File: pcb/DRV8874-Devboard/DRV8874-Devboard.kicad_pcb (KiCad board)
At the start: 4 copper layers, 65 x 67 mm, 53 parts, among them J1 Conn_01x04_Pin, J10 Conn_01x06_Pin, J12 Conn_01x03_Pin, J2 Screw_Terminal_01x02, J3 Conn_01x03_Pin, J4 Conn_01x03_Pin, J5 Conn_01x04_Pin, J6 Conn_01x03_Pin, J7 Conn_01x03_Pin, J9 Conn_01x03_Pin, U1 DRV8874, U2 BL9342, U3 DRV8874, U4 SN65HVD230, U5 TPS16630PWPR, U6 M95320-WMN6TP, U7 TinyThinker_J1

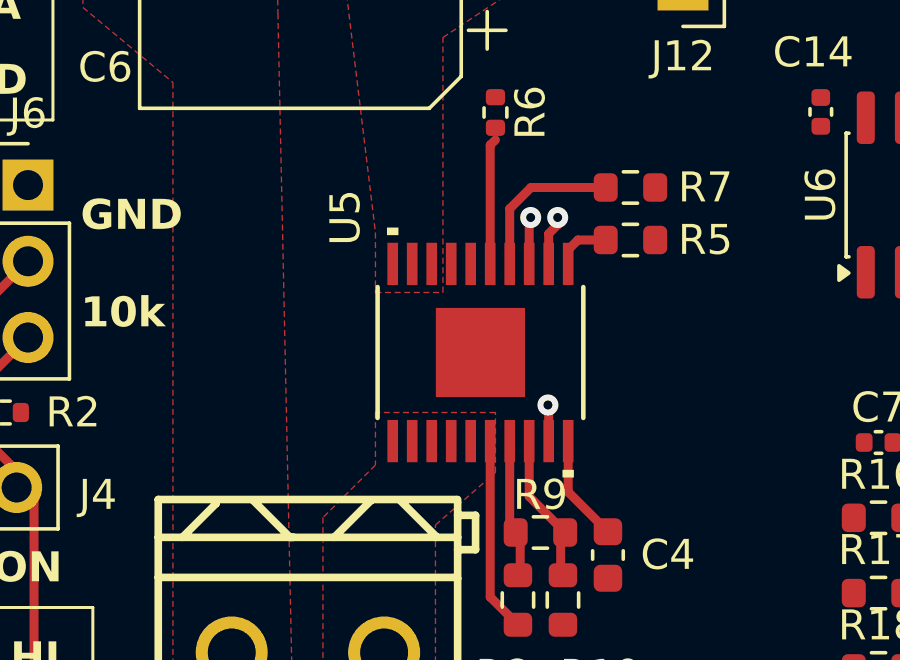
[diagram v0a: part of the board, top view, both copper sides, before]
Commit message: updated rotation offsets
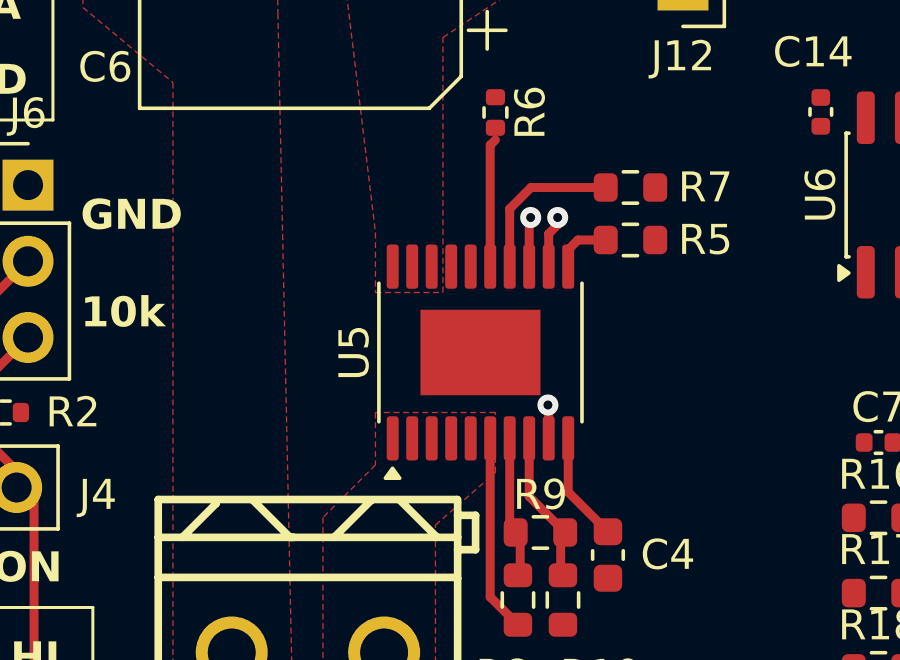
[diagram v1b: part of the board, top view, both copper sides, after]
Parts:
- U5: footprint Custom_Library:HTSSOP20_PWP_TEX -> Package_SO:HTSSOP-20-1EP_4.4x6.5mm_P0.65mm_EP2.85x4mm

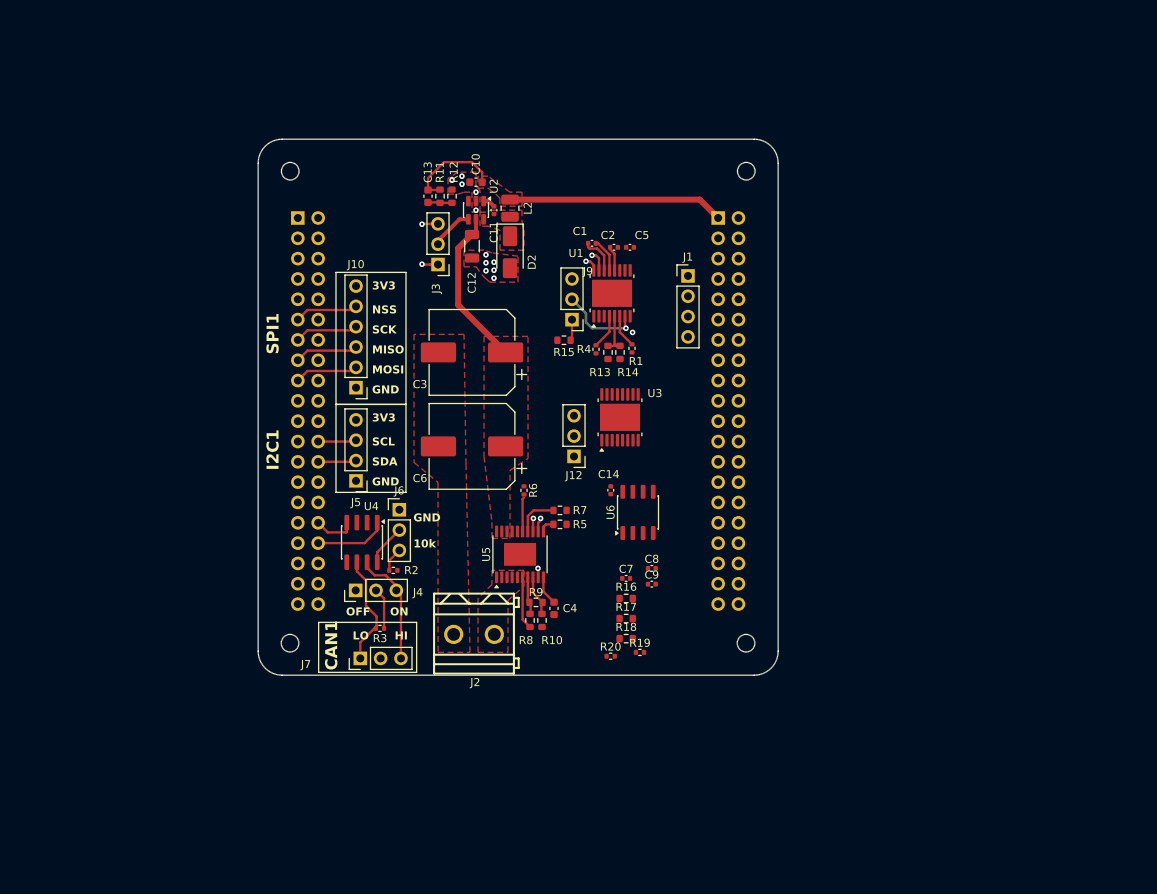
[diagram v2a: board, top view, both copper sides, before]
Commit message: routed major chunk of DRV8874 pair
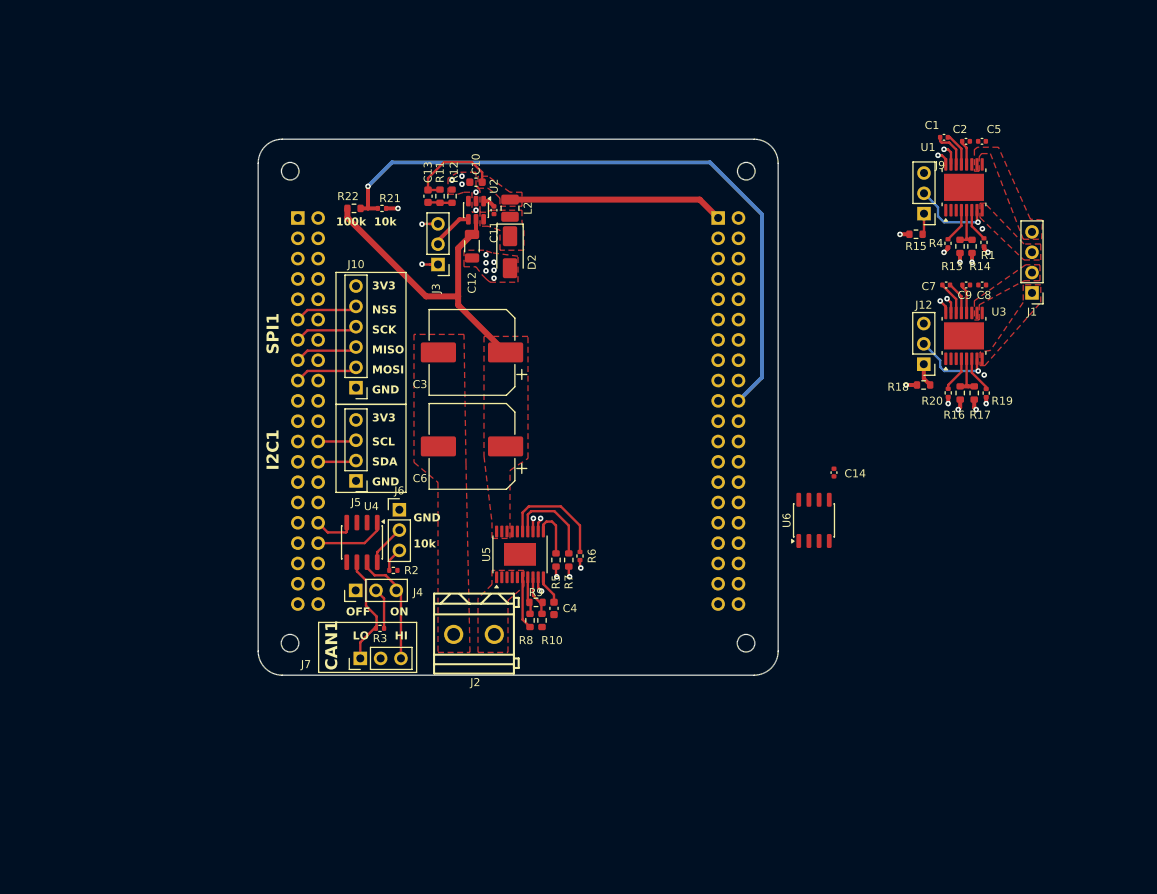
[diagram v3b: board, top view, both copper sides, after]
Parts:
- added R21: 10k, Resistor_SMD:R_0402_1005Metric, F.Cu at (112.2, 48.2)
- added R22: 100k, Resistor_SMD:R_0603_1608Metric, F.Cu at (108.8, 48.2)
- moved C8 54.4 mm to (187.3, 57.8)
- moved C7 54.3 mm to (182.8, 57.8), turned to 180 degrees
- moved C9 54.2 mm to (185.3, 57.8), turned to 180 degrees
- moved R19 54.1 mm to (187.8, 71.3), turned to -90 degrees
- moved R20 53.5 mm to (183.0, 71.3), turned to 90 degrees
- moved R17 51.8 mm to (186.3, 71.3), turned to -90 degrees
- moved R16 49.0 mm to (184.5, 71.3), turned to 90 degrees
- moved R18 48.9 mm to (179.9, 70.3), turned to 180 degrees
- moved C1 46.0 mm to (182.5, 39.4)
- moved C2 46.0 mm to (185.2, 39.9)
- moved C5 46.0 mm to (187.2, 39.9)
- moved J9 46.0 mm to (180.0, 48.9)
- moved R1 46.0 mm to (187.5, 52.5)
- moved R13 46.0 mm to (184.5, 53.0)
- moved R14 46.0 mm to (186.0, 53.0)
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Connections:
- J1 pad 1: /B_OUT- -> /B_OUT+
- J1 pad 2: /A_OUT- -> /B_OUT-
- J1 pad 3: /B_OUT+ -> /A_OUT+
- J1 pad 4: /A_OUT+ -> /A_OUT-
- U7 pad 20: unconnected-(U7A-ADC1_IN8-Pad20) -> /ADC_VSENSE
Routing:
- net /ADC_VSENSE: track 0.00 -> 82.3 mm, vias 0 -> 1
- net +BATT_PROT: track 19.8 -> 38.9 mm
- net GND: track 7.44 -> 21.1 mm, vias 16 -> 27
- net /B_IMODE: track 0.00 -> 10.3 mm, vias 0 -> 1
- net /TPS_FLT: track 4.21 -> 14.1 mm
- net +3.3V: track 5.42 -> 12.4 mm, vias 3 -> 9
- net /TPS_MON: track 5.33 -> 11.6 mm
- net /B_VREF: track 0.00 -> 5.28 mm
- net /TPS_ILIM: track 1.86 -> 6.75 mm
- net /B_IRPOPI: track 0.00 -> 4.52 mm
- net /B_nFault: track 0.00 -> 4.44 mm
- net /B_CPL: track 0.00 -> 4.23 mm
- net /B_CPH: track 0.00 -> 4.10 mm
- net /B_VCP: track 0.00 -> 3.72 mm
- net /B_IMODE_R: track 0.00 -> 2.93 mm
- added copper zone on F.Cu, net /A_OUT+
- added copper zone on F.Cu, net /A_OUT-
- added copper zone on F.Cu, net /B_OUT+
- added copper zone on F.Cu, net /B_OUT-
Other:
- board text added: "100k"

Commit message: moved DRV8874 pair onto the board
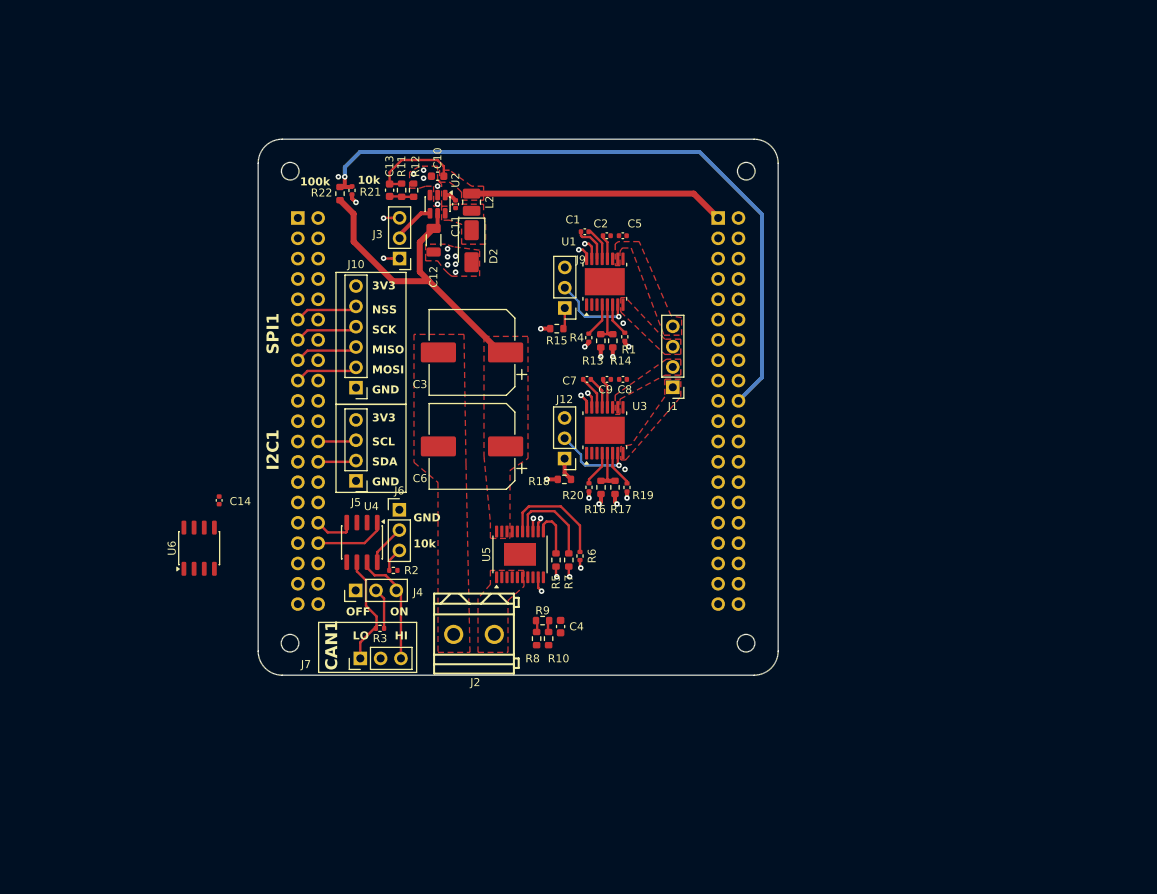
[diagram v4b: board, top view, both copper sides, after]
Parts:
- moved C14 76.9 mm to (91.9, 84.7)
- moved U6 76.9 mm to (89.4, 90.7)
- moved J12 46.4 mm to (135.1, 79.5)
- moved C1 46.4 mm to (137.6, 51.2)
- moved C2 46.4 mm to (140.3, 51.7)
- moved C5 46.4 mm to (142.3, 51.7)
- moved C7 46.4 mm to (137.9, 69.6)
- moved C8 46.4 mm to (142.4, 69.6)
- moved C9 46.4 mm to (140.4, 69.6)
- moved J1 46.4 mm to (148.6, 70.6)
- moved J9 46.4 mm to (135.1, 60.7)
- moved R1 46.4 mm to (142.6, 64.3)
- moved R13 46.4 mm to (139.6, 64.8)
- moved R14 46.4 mm to (141.1, 64.8)
- moved R15 46.4 mm to (134.1, 63.3)
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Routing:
- net +BATT_RAW: track 6.51 -> 0.00 mm
- net +5V: track 39.3 -> 44.0 mm
- net /TPS_OVP: track 5.30 -> 1.56 mm
- net /TPS_DVDT: track 3.57 -> 0.00 mm
- net /TPS_UVLO: track 4.69 -> 1.85 mm
- net /ADC_VSENSE: track 82.3 -> 84.7 mm
- net +BATT_PROT: track 38.9 -> 40.3 mm
- net GND: track 21.1 -> 20.8 mm, vias 27 -> 28

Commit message: checkpoint
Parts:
- moved U6 54.1 mm to (143.2, 96.7)
- moved C14 53.7 mm to (145.3, 90.6)
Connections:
- U7 pad 29: unconnected-(U7A-TIM2_CH4-Pad29) -> /A_IN1
- U7 pad 32: unconnected-(U7A-TIM2_CH1-Pad32) -> /A_IN2
- U7 pad 33: unconnected-(U7A-TIM2_CH2-Pad33) -> /B_IN1
- U7 pad 36: unconnected-(U7A-TIM2_CH3-Pad36) -> /B_IN2

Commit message: changed color of phase B net
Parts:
- moved C14 7.53 mm to (145.5, 98.1)
- moved U6 1.84 mm to (142.0, 98.1)
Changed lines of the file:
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@@
 	(footprint "Package_SO:SO-8_3.9x4.9mm_P1.27mm"
 		(layer "F.Cu")
-		(at 143.2 96.7 90)
+		(at 142 98.1 90)
 		(descr "SO, 8 Pin (https://www.nxp.com/docs/en/data-sheet/PCF8523.pdf), generated with kicad-footprint-generator ipc_gullwing_generator.py")
 		(tags "SO SO")
@@
 	(footprint "Capacitor_SMD:C_0402_1005Metric"
 		(layer "F.Cu")
-		(at 145.265 90.595 -90)
+		(at 145.5 98.12 -90)
 		(descr "Capacitor SMD 0402 (1005 Metric), square (rectangular) end terminal, IPC-7351 nominal, (Body size source: IPC-SM-782 page 76, https://www.pcb-3d.com/wordpress/wp-content/uploads/ipc-sm-782a_amendment_1_and_2.pdf), generated with kicad-footprint-generator")
 		(tags "capacitor")

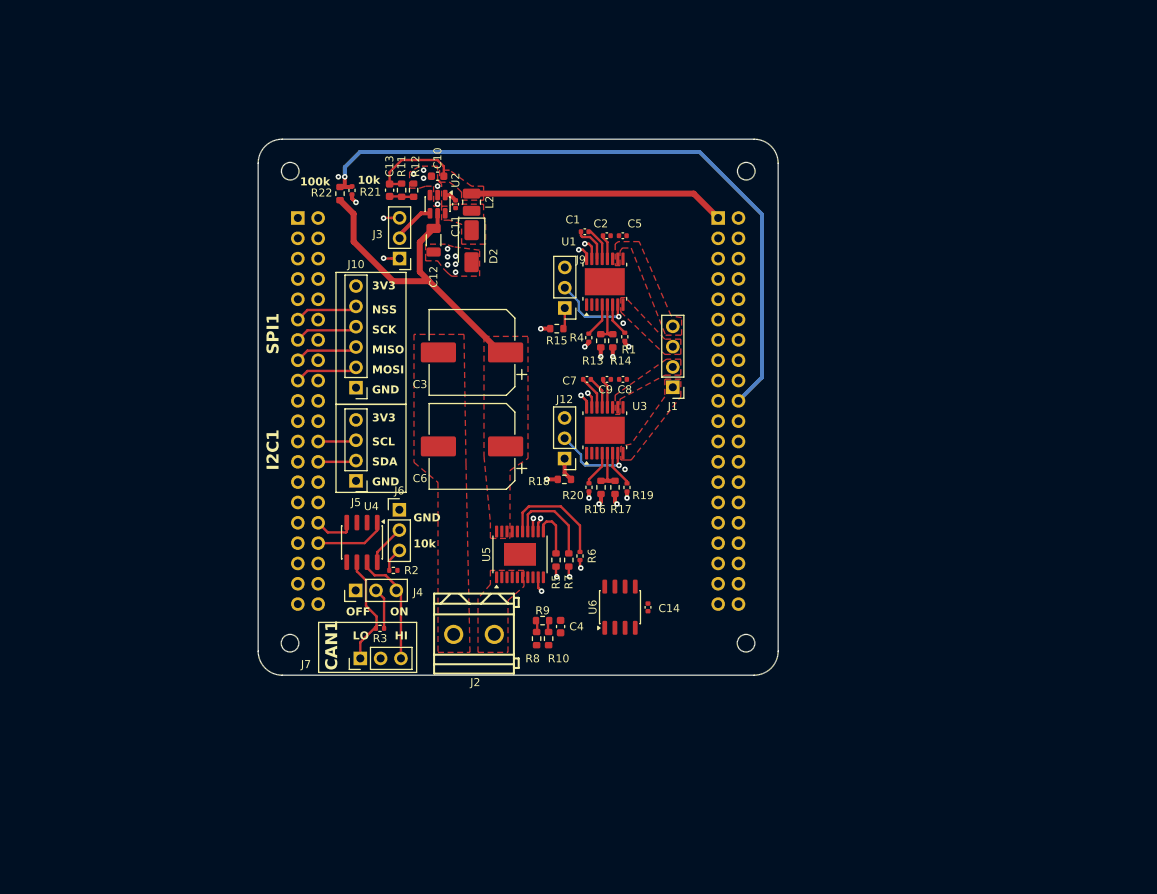
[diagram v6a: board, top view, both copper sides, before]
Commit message: added GND and 3.3V fills
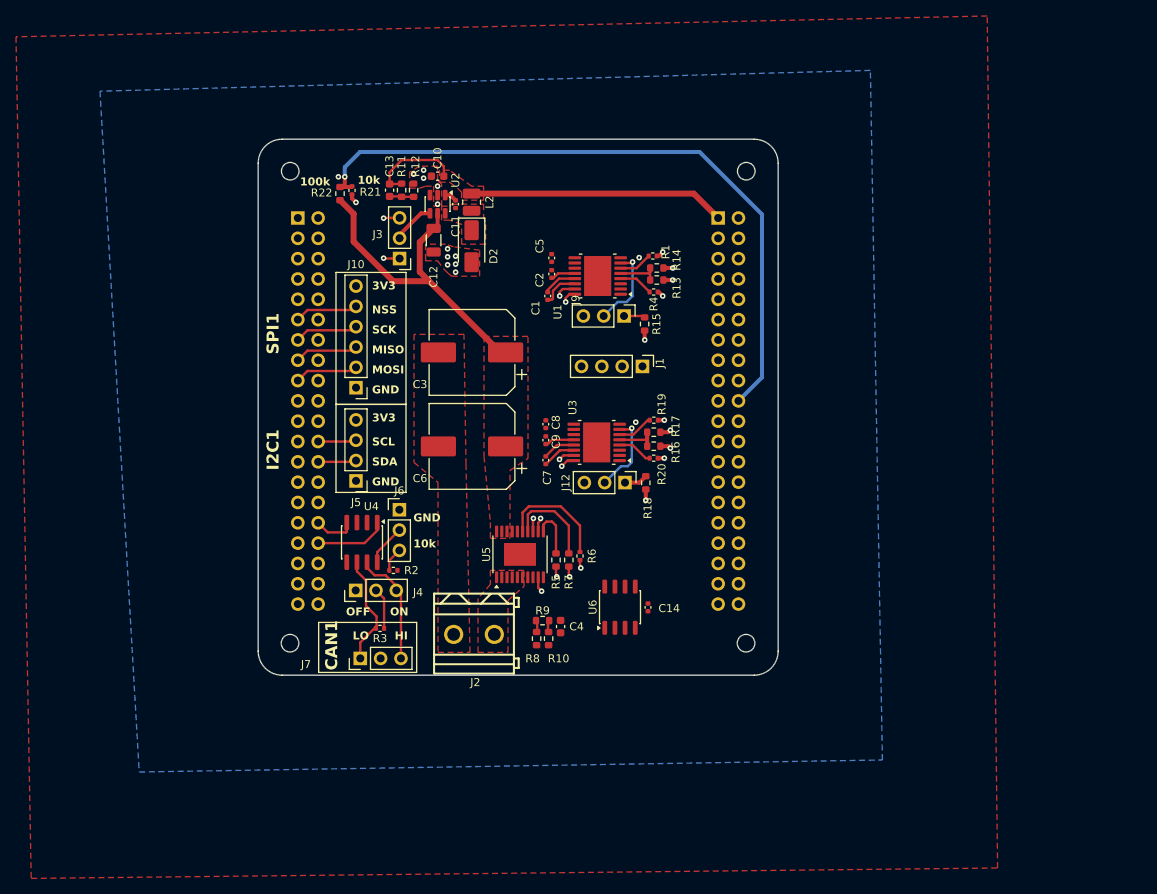
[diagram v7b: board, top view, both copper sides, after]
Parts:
- moved C7 11.3 mm to (132.7, 79.7), turned to -90 degrees
- moved C8 11.2 mm to (132.7, 75.2), turned to 90 degrees
- moved R15 11.0 mm to (145.1, 62.7), turned to -90 degrees
- moved C9 10.8 mm to (132.7, 77.2), turned to -90 degrees
- moved R1 10.7 mm to (146.1, 54.2), turned to 0 degrees
- moved R14 10.6 mm to (146.6, 55.7), turned to 0 degrees
- moved R13 10.3 mm to (146.6, 57.2), turned to 180 degrees
- moved R18 10.2 mm to (145.2, 82.5), turned to -90 degrees
- moved R4 9.92 mm to (146.2, 58.7), turned to 180 degrees
- moved C5 9.31 mm to (133.5, 54.5), turned to 90 degrees
- moved C1 9.28 mm to (133.0, 59.2), turned to -90 degrees
- moved R19 9.05 mm to (146.2, 74.7), turned to 0 degrees
- moved R20 8.87 mm to (146.2, 79.5), turned to 180 degrees
- moved R17 8.43 mm to (146.2, 76.2), turned to 0 degrees
- moved C2 8.39 mm to (133.5, 56.5), turned to -90 degrees
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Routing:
- added copper zone on B.Cu, net +3.3V
- added copper zone on In1.Cu, net GND
- added copper zone on In2.Cu, net GND
- removed copper zone on F.Cu, net /A_OUT+
- removed copper zone on F.Cu, net /A_OUT-
- removed copper zone on F.Cu, net /B_OUT+
- removed copper zone on F.Cu, net /B_OUT-
